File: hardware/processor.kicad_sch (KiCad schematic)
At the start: 15 parts, among them U1 ESP32-PICO-V3-02

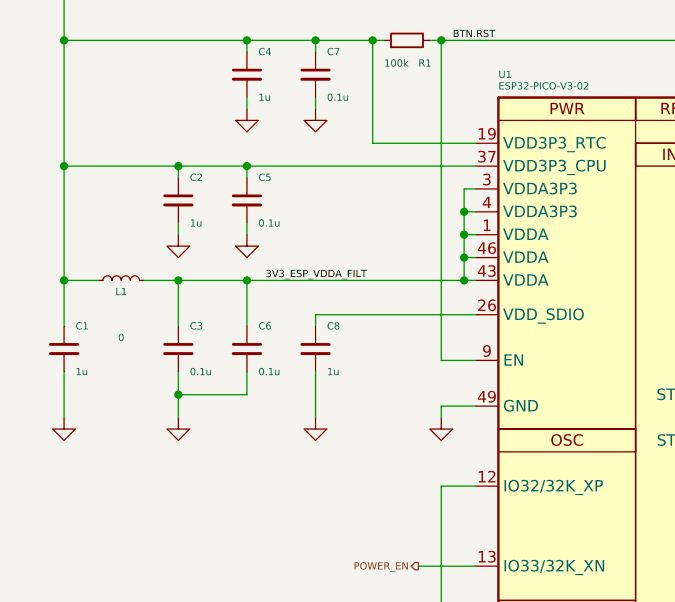
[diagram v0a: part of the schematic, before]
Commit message: schematic tidy up, component placement, shielding investigation
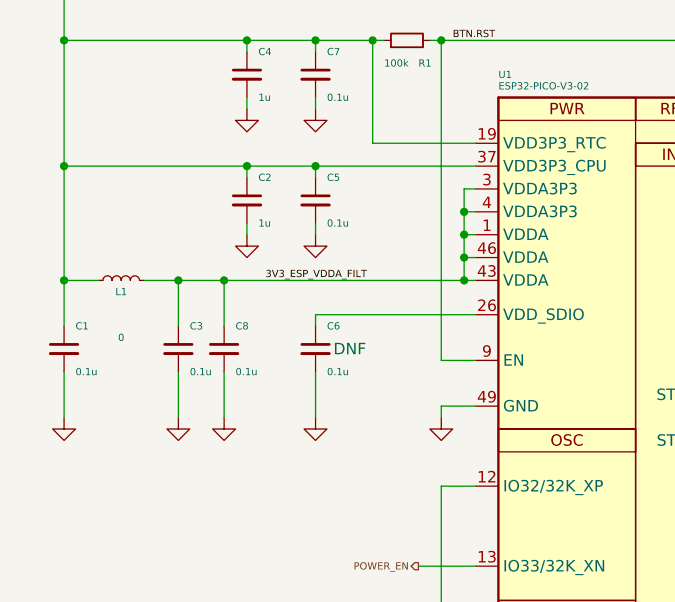
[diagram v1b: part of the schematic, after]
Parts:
- AE1: footprint RF_Antenna:Texas_SWRA117D_2.4GHz_Left -> RF_Antenna:Johanson_2450AT18x100
- C1: value 1u -> 0.1u; footprint Capacitor_SMD:C_0603_1608Metric -> Capacitor_SMD:C_0402_1005Metric
- C6: DNF (none) -> DNF
- C8: value 1u -> 0.1u; footprint Capacitor_SMD:C_0603_1608Metric -> Capacitor_SMD:C_0402_1005Metric; Voltage 15V -> 50V
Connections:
- net 3V3_ESP_VDDA_FILT: now also C8.1; no longer C6.1
- net at U1.26 (VDD_SDIO): now also C6.1; no longer C8.1
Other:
- moved on the sheet: C2, C5

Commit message: minor sch tweaks, more layout, added power emc shield
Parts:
- C2, C4: footprint Capacitor_SMD:C_0603_1608Metric -> Capacitor_SMD:C_0402_1005Metric
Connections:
- net GND: no longer AE1.2 (PCB_Trace)
- net at C10.1, L2.2: now also AE1.2 (PCB_Trace); no longer AE1.1 (FEED)
- net 3V3_CORE renamed VDD_CORE_3V3
- no-connect marks 4 -> 5
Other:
- moved on the sheet: AE1
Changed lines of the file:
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@@
   (no_connect (at 120.65 130.81))
   (no_connect (at 120.65 123.19))
+  (no_connect (at 205.74 45.72))
   (bus_entry (at 219.71 100.33) (size -2.54 2.54)
     (stroke (width 0) (type default) (color 0 0 0 0))
@@
   )
   (wire (pts (xy 110.49 55.88) (xy 109.22 55.88))
-    (stroke (width 0) (type default) (color 0 0 0 0))
-  )
-  (wire (pts (xy 205.74 54.61) (xy 205.74 45.72))
     (stroke (width 0) (type default) (color 0 0 0 0))
   )
@@
     (pin "2")
   )
-  (symbol (lib_id "power:GND") (at 205.74 54.61 0) (unit 1)
-    (in_bom yes) (on_board yes) (fields_autoplaced)
-    (property "Reference" "#PWR011" (id 0) (at 205.74 60.96 0)
-      (effects (font (size 0.8 0.8)) hide)
-    )
-    (property "Value" "GND" (id 1) (at 205.74 59.69 0)
-      (effects (font (size 0.8 0.8)) hide)
-    )
-    (property "Footprint" "" (id 2) (at 205.74 54.61 0)
-      (effects (font (size 0.8 0.8)) hide)
-    )
-    (property "Datasheet" "" (id 3) (at 205.74 54.61 0)
-      (effects (font (size 0.8 0.8)) hide)
-    )
-    (pin "1")
-  )
   (symbol (lib_id "power:GND") (at 116.84 97.79 0) (unit 1)
     (in_bom yes) (on_board yes) (fields_autoplaced)
@@
     (pin "1")
   )
-  (symbol (lib_id "Device:Antenna_Chip") (at 203.2 43.18 0) (unit 1)
+  (symbol (lib_id "Device:Antenna_Chip") (at 203.2 43.18 0) (mirror y) (unit 1)
     (in_bom yes) (on_board yes) (fields_autoplaced)
-    (property "Reference" "AE1" (id 0) (at 208.28 40.005 0)
-      (effects (font (size 0.8 0.8)) (justify left))
-    )
-    (property "Value" "2.4G" (id 1) (at 208.28 42.545 0)
-      (effects (font (size 0.8 0.8)) (justify left))
-    )
-    (property "Footprint" "RF_Antenna:Johanson_2450AT18x100" (id 2) (at 200.66 38.735 0)
-      (effects (font (size 0.8 0.8)) hide)
-    )
-    (property "Datasheet" "~" (id 3) (at 200.66 38.735 0)
+    (property "Reference" "AE1" (id 0) (at 207.01 40.005 0)
+      (effects (font (size 0.8 0.8)) (justify right))
+    )
+    (property "Value" "2.4G" (id 1) (at 207.01 42.545 0)
+      (effects (font (size 0.8 0.8)) (justify right))
+    )
+    (property "Footprint" "RF_Antenna:Johanson_2450AT18x100" (id 2) (at 205.74 38.735 0)
+      (effects (font (size 0.8 0.8)) hide)
+    )
+    (property "Datasheet" "~" (id 3) (at 205.74 38.735 0)
       (effects (font (size 0.8 0.8)) hide)
     )
@@
       (effects (font (size 0.8 0.8)) (justify left))
     )
-    (property "Footprint" "Capacitor_SMD:C_0603_1608Metric" (id 2) (at 95.25 59.69 0)
+    (property "Footprint" "Capacitor_SMD:C_0402_1005Metric" (id 2) (at 95.25 59.69 0)
       (effects (font (size 0.8 0.8)) hide)
     )
@@
       (effects (font (size 0.8 0.8)) (justify left))
     )
-    (property "Footprint" "Capacitor_SMD:C_0603_1608Metric" (id 2) (at 95.25 73.66 0)
-      (effects (font (size 0.8 0.8)) hide)
-    )
+    (property "Footprint" "Capacitor_SMD:C_0402_1005Metric" (id 2) (at 95.25 73.66 0)
+      (effects (font (size 0.8 0.8)) hide)
+    )

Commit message: Updates
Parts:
- removed AE1: 2.4G, RF_Antenna:Johanson_2450AT18x100, symbol Device:Antenna_Chip
- removed C1, C10, C3, C5, C6, C7, C8, C9: 0.1u, Capacitor_SMD:C_0402_1005Metric, symbol Device:C_Small
- removed C2, C4: 1u, Capacitor_SMD:C_0402_1005Metric, symbol Device:C_Small
- removed L1: 0, Resistor_SMD:R_0402_1005Metric, symbol Device:L_Small
- removed L2: L_Small, Inductor_SMD:L_0402_1005Metric, symbol Device:L_Small
- removed R1: 100k, Resistor_SMD:R_0402_1005Metric, symbol Device:R_Small
- removed U1: ESP32-PICO-V3-02, Package_DFN_QFN:QFN-48-1EP_7x7mm_P0.5mm_EP5.3x5.3mm, symbol bt_MCU_Espressif:ESP32-PICO-V3-02
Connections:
- no-connect marks 5 -> 0
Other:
- note removed: "50R Impedance Controlled"
- note removed: "Provide a large surrounding ground plane and away from inteference."

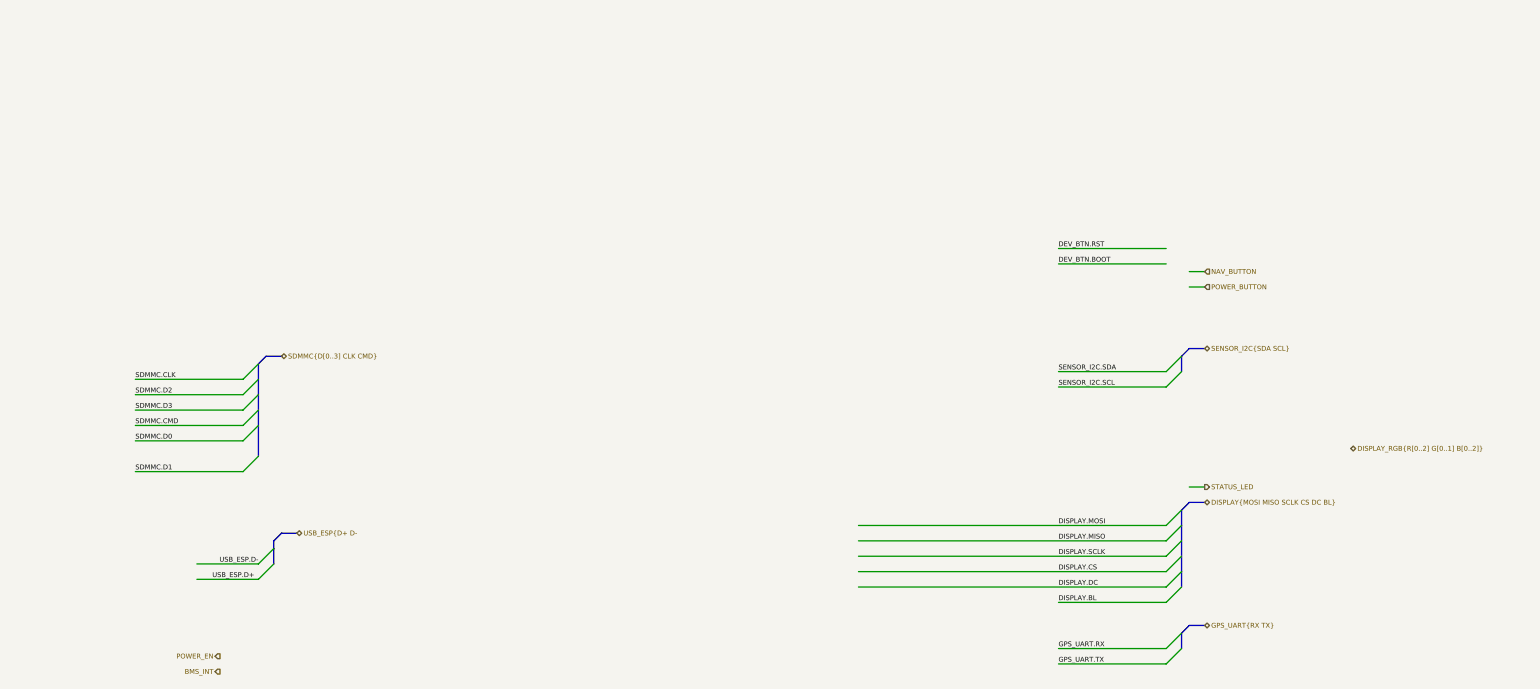
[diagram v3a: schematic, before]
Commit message: Added ESP32-S3-WROOM
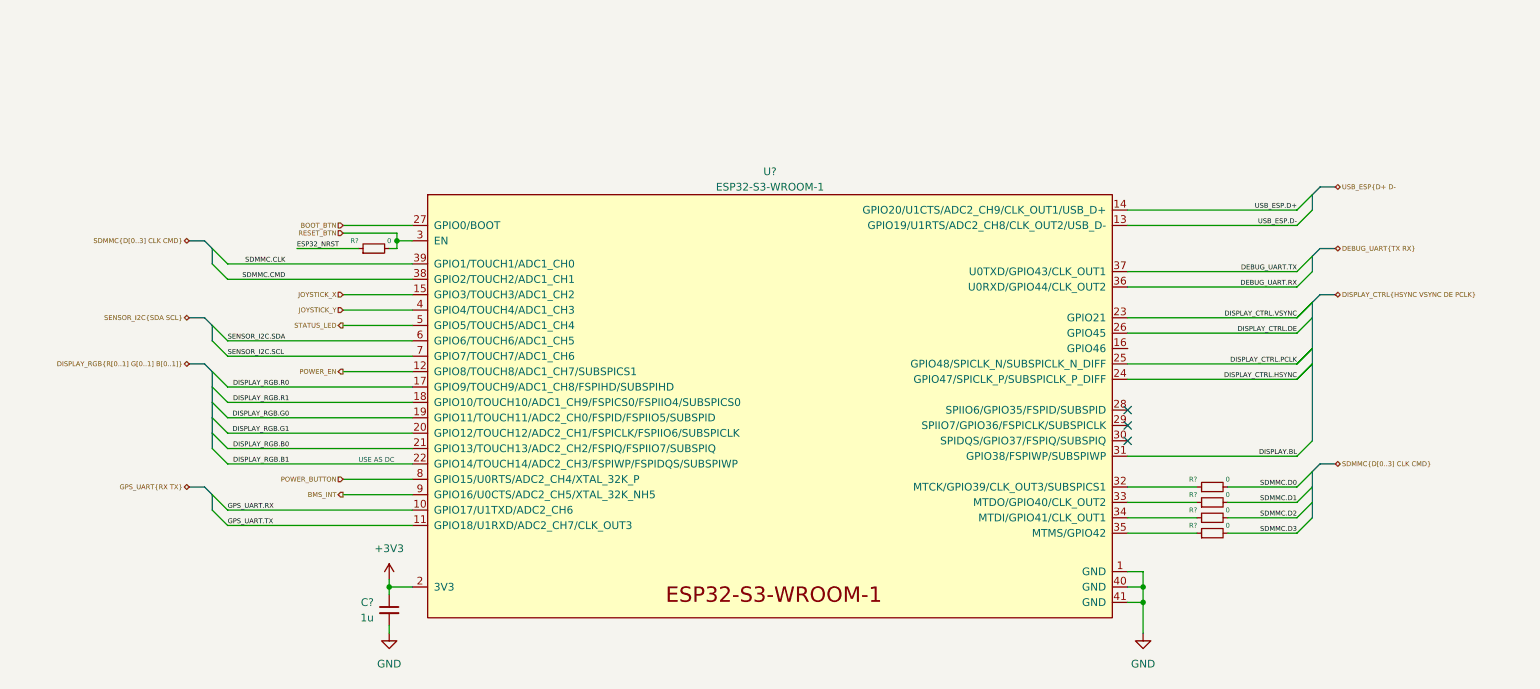
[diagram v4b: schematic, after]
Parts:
- added C?: 1u, symbol Device:C_Small
- added R? (x5): 0, symbol Device:R_Small
- added U?: ESP32-S3-WROOM-1, bt_Espressif:ESP32-S3-WROOM-1, symbol bt_Espressif:ESP32-S3-WROOM-1
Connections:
- net BMS_INT: now also U?.9 (GPIO16/U0CTS/ADC2_CH5/XTAL_32K_NH5)
- net DISPLAY.BL: now also U?.31 (GPIO38/FSPIWP/SUBSPIWP)
- net GPS_UART.RX: now also U?.10 (GPIO17/U1TXD/ADC2_CH6)
- net GPS_UART.TX: now also U?.11 (GPIO18/U1RXD/ADC2_CH7/CLK_OUT3)
- net POWER_BUTTON: now also U?.8 (GPIO15/U0RTS/ADC2_CH4/XTAL_32K_P)
- net POWER_EN: now also U?.12 (GPIO8/TOUCH8/ADC1_CH7/SUBSPICS1)
- net SDMMC.CLK: now also U?.39 (GPIO1/TOUCH1/ADC1_CH0)
- net SDMMC.CMD: now also U?.38 (GPIO2/TOUCH2/ADC1_CH1)
- net SDMMC.D0: now also R?.2
- net SDMMC.D1: now also R?.2
- net SDMMC.D2: now also R?.2
- net SDMMC.D3: now also R?.2
- net SENSOR_I2C.SCL: now also U?.7 (GPIO7/TOUCH7/ADC1_CH6)
- net SENSOR_I2C.SDA: now also U?.6 (GPIO6/TOUCH6/ADC1_CH5)
- net STATUS_LED: now also U?.5 (GPIO5/TOUCH5/ADC1_CH4)
- net USB_ESP.D+: now also U?.14 (GPIO20/U1CTS/ADC2_CH9/CLK_OUT1/USB_D+)
- net USB_ESP.D-: now also U?.13 (GPIO19/U1RTS/ADC2_CH8/CLK_OUT2/USB_D-)
- new net: R?.1, U?.32 (MTCK/GPIO39/CLK_OUT3/SUBSPICS1)
- new net: R?.1, U?.33 (MTDO/GPIO40/CLK_OUT2)
- new net: R?.1, U?.34 (MTDI/GPIO41/CLK_OUT1)
- new net: R?.1, U?.35 (MTMS/GPIO42)
- new net +3V3: C?.1, U?.2 (3V3)
- new net BOOT_BTN: U?.27 (GPIO0/BOOT)
- new net DEBUG_UART.RX: U?.36 (U0RXD/GPIO44/CLK_OUT2)
- new net DEBUG_UART.TX: U?.37 (U0TXD/GPIO43/CLK_OUT1)
- new net DISPLAY_CTRL.DE: U?.26 (GPIO45)
- new net DISPLAY_CTRL.HSYNC: U?.24 (GPIO47/SPICLK_P/SUBSPICLK_P_DIFF)
- new net DISPLAY_CTRL.PCLK: U?.25 (GPIO48/SPICLK_N/SUBSPICLK_N_DIFF)
- new net DISPLAY_CTRL.VSYNC: U?.23 (GPIO21)
- new net DISPLAY_RGB.B0: U?.21 (GPIO13/TOUCH13/ADC2_CH2/FSPIQ/FSPIIO7/SUBSPIQ)
- new net DISPLAY_RGB.B1: U?.22 (GPIO14/TOUCH14/ADC2_CH3/FSPIWP/FSPIDQS/SUBSPIWP)
- new net DISPLAY_RGB.G0: U?.19 (GPIO11/TOUCH11/ADC2_CH0/FSPID/FSPIIO5/SUBSPID)
- new net DISPLAY_RGB.G1: U?.20 (GPIO12/TOUCH12/ADC2_CH1/FSPICLK/FSPIIO6/SUBSPICLK)
- new net DISPLAY_RGB.R0: U?.17 (GPIO9/TOUCH9/ADC1_CH8/FSPIHD/SUBSPIHD)
- new net DISPLAY_RGB.R1: U?.18 (GPIO10/TOUCH10/ADC1_CH9/FSPICS0/FSPIIO4/SUBSPICS0)
- new net ESP32_NRST: R?.1
- new net GND: C?.2, U?.1 (GND), U?.40 (GND), U?.41 (GND)
- new net JOYSTICK_X: U?.15 (GPIO3/TOUCH3/ADC1_CH2)
- new net JOYSTICK_Y: U?.4 (GPIO4/TOUCH4/ADC1_CH3)
- new net RESET_BTN: R?.2, U?.3 (EN)
- no-connect marks 0 -> 3
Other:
- note added: "USE AS DC"

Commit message: changing sdmmc to spi to support lcd rgb mode
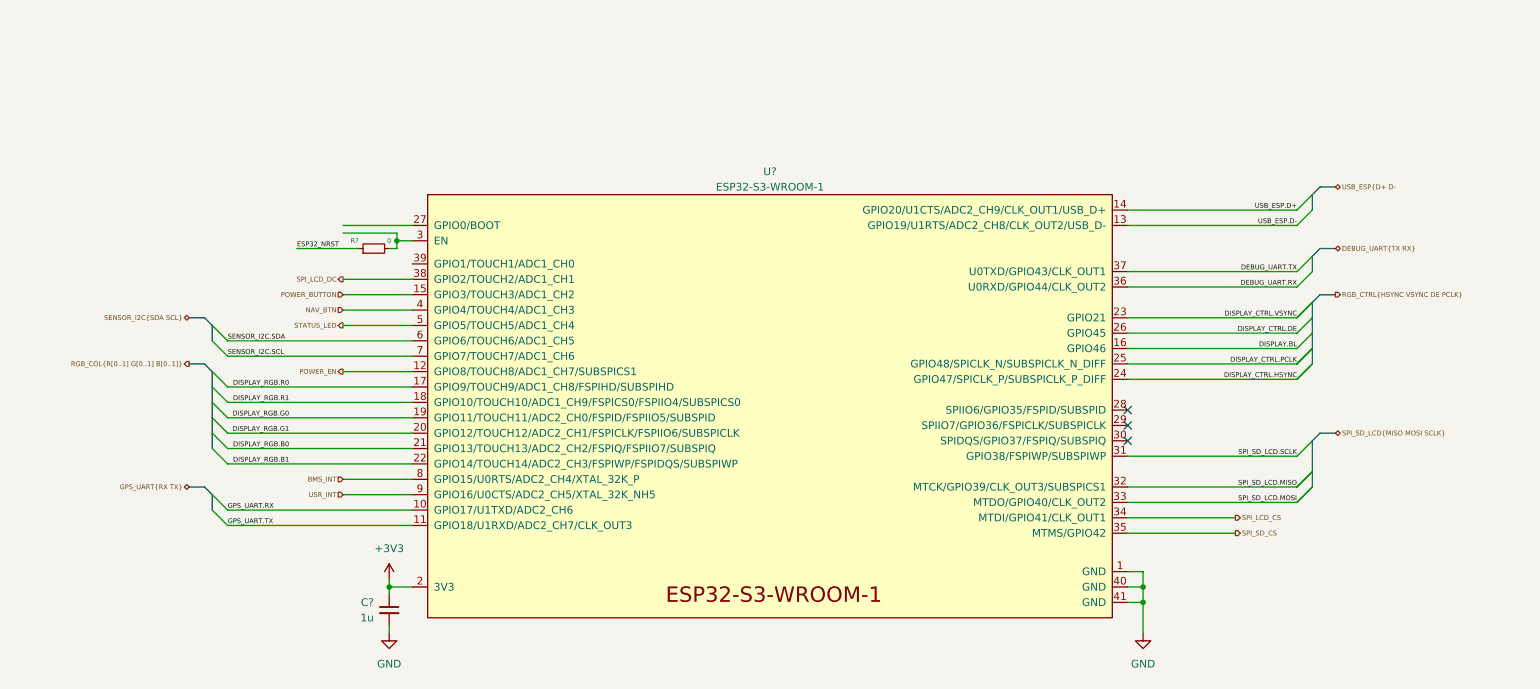
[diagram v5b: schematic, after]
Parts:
- removed R? (x4): 0, symbol Device:R_Small
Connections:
- net JOYSTICK_X is gone; now on net POWER_BUTTON: U?.15 (GPIO3/TOUCH3/ADC1_CH2)
- net BMS_INT: now also U?.8 (GPIO15/U0RTS/ADC2_CH4/XTAL_32K_P); no longer U?.9 (GPIO16/U0CTS/ADC2_CH5/XTAL_32K_NH5)
- net DISPLAY.BL: now also U?.16 (GPIO46); no longer U?.31 (GPIO38/FSPIWP/SUBSPIWP)
- net POWER_BUTTON: no longer U?.8 (GPIO15/U0RTS/ADC2_CH4/XTAL_32K_P)
- net SPI_SD_LCD.MISO: now reaches U?.32 (MTCK/GPIO39/CLK_OUT3/SUBSPICS1)
- net SPI_SD_LCD.MOSI: now reaches U?.33 (MTDO/GPIO40/CLK_OUT2)
- net SPI_LCD_CS: now reaches U?.34 (MTDI/GPIO41/CLK_OUT1)
- net SPI_SD_CS: now reaches U?.35 (MTMS/GPIO42)
- net BOOT_BTN: no longer names the net of U?.27 (GPIO0/BOOT)
- net JOYSTICK_Y renamed NAV_BTN
- net RESET_BTN: no longer names the net of R?.2, U?.3 (EN)
- net SDMMC.CLK: no longer names the net of U?.39 (GPIO1/TOUCH1/ADC1_CH0)
- net SDMMC.CMD renamed SPI_LCD_DC
- new net SPI_SD_LCD.SCLK: U?.31 (GPIO38/FSPIWP/SUBSPIWP)
- new net USR_INT: U?.9 (GPIO16/U0CTS/ADC2_CH5/XTAL_32K_NH5)
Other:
- note removed: "USE AS DC"
